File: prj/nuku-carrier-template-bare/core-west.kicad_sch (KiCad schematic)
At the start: 3 parts, among them J3 DF40HC(4.0)-90DS-0.4V

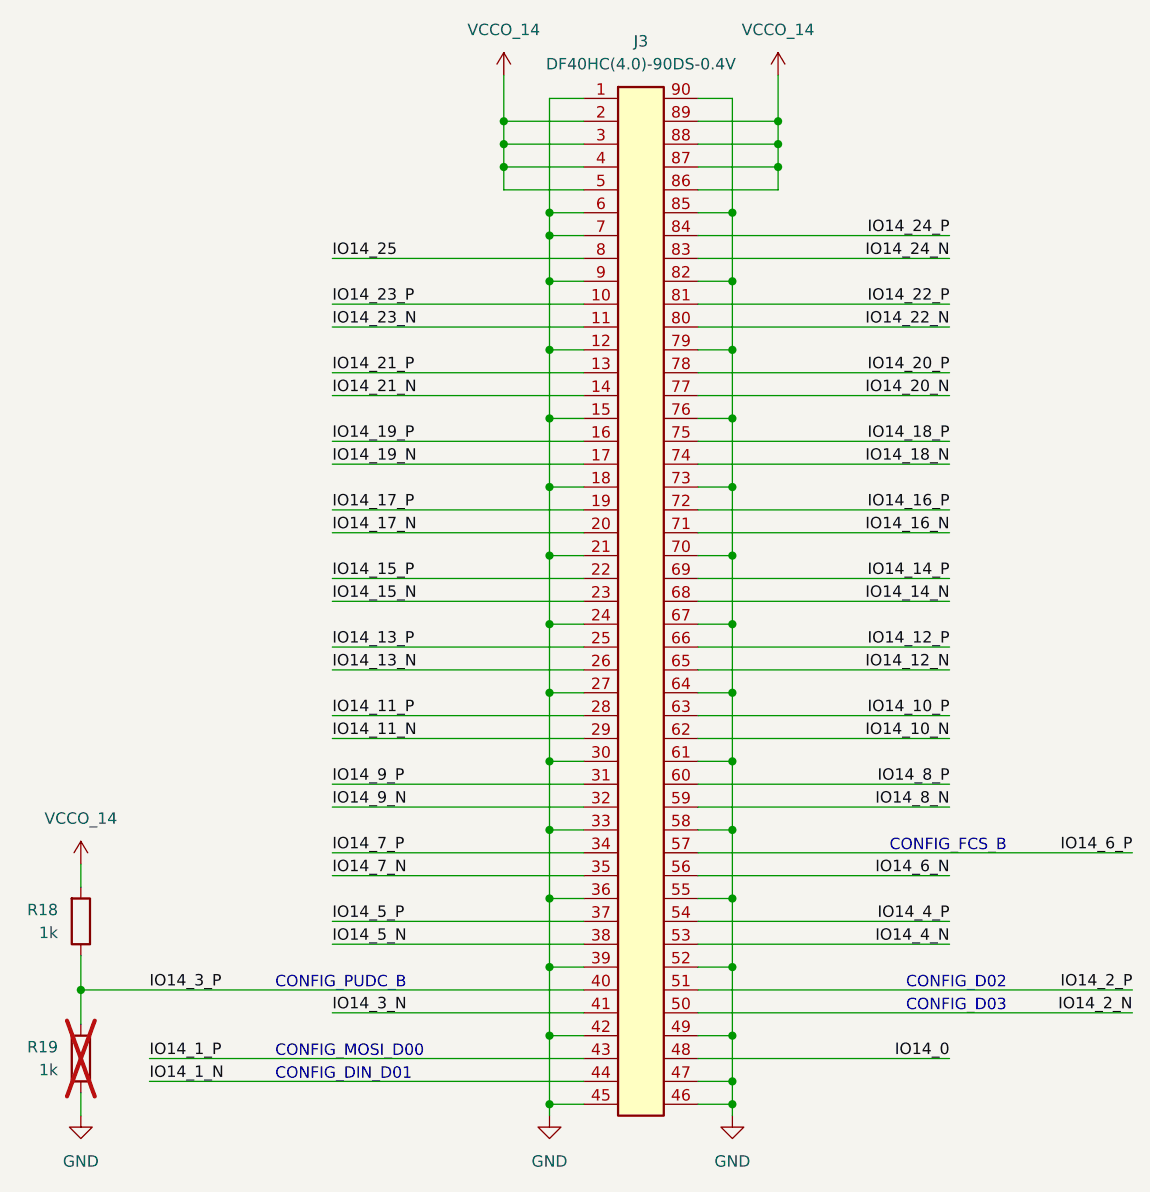
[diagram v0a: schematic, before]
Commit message: Update nuku.carrier.template to template.bare
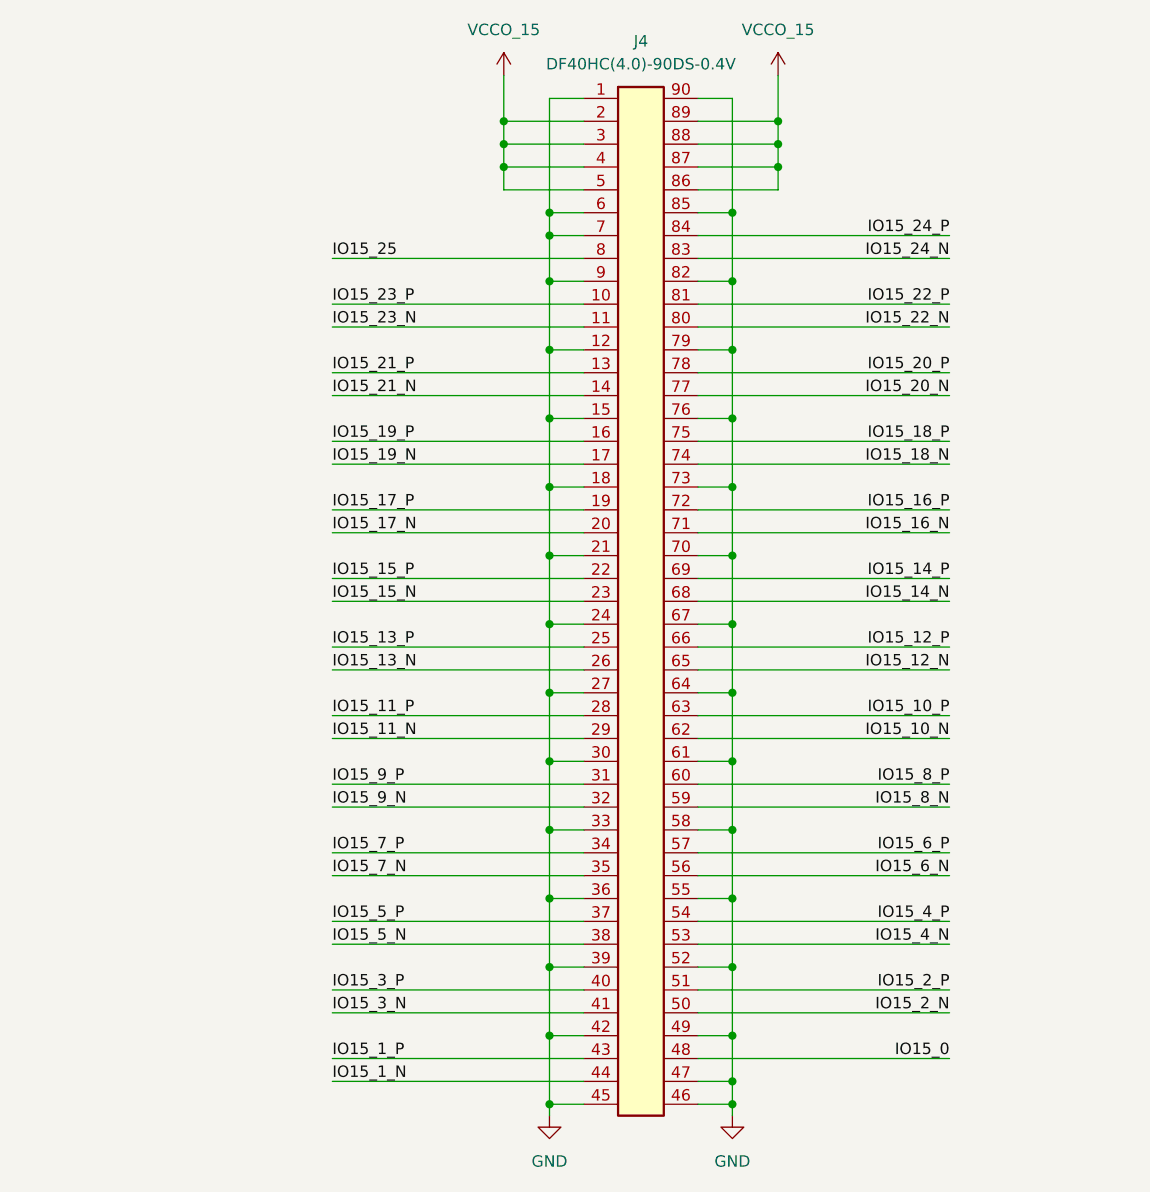
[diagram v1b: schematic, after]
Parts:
- removed J3: DF40HC(4.0)-90DS-0.4V, nuku:DF40HC(4.0)-90DS-0.4V, symbol nuku:DF40HC(4.0)-90DS-0.4V
- removed R18, R19: 1k, Resistor_SMD:R_0402_1005Metric, symbol Device:R
- added J4: DF40HC(4.0)-90DS-0.4V, nuku:DF40HC(4.0)-90DS-0.4V, symbol nuku:DF40HC(4.0)-90DS-0.4V
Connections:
- net GND: now also J4.1, J4.12, J4.15, J4.18, J4.21, J4.24, J4.27, J4.30, J4.33, J4.36, J4.39, J4.42, J4.45, J4.46, J4.47, J4.49, J4.52, J4.55, J4.58, J4.6, J4.61, J4.64, J4.67, J4.7, J4.70, J4.73, J4.76, J4.79, J4.82, J4.85, J4.9, J4.90
- new net IO15_0: J4.48
- new net IO15_10_N: J4.62
- new net IO15_10_P: J4.63
- new net IO15_11_N: J4.29
- new net IO15_11_P: J4.28
- new net IO15_12_N: J4.65
- new net IO15_12_P: J4.66
- new net IO15_13_N: J4.26
- new net IO15_13_P: J4.25
- new net IO15_14_N: J4.68
- new net IO15_14_P: J4.69
- new net IO15_15_N: J4.23
- new net IO15_15_P: J4.22
- new net IO15_16_N: J4.71
- new net IO15_16_P: J4.72
- new net IO15_17_N: J4.20
- new net IO15_17_P: J4.19
- new net IO15_18_N: J4.74
- new net IO15_18_P: J4.75
- new net IO15_19_N: J4.17
- new net IO15_19_P: J4.16
- new net IO15_1_N: J4.44
- new net IO15_1_P: J4.43
- new net IO15_20_N: J4.77
- new net IO15_20_P: J4.78
- new net IO15_21_N: J4.14
- new net IO15_21_P: J4.13
- new net IO15_22_N: J4.80
- new net IO15_22_P: J4.81
- new net IO15_23_N: J4.11
- new net IO15_23_P: J4.10
- new net IO15_24_N: J4.83
- new net IO15_24_P: J4.84
- new net IO15_25: J4.8
- new net IO15_2_N: J4.50
- new net IO15_2_P: J4.51
- new net IO15_3_N: J4.41
- new net IO15_3_P: J4.40
- new net IO15_4_N: J4.53
- new net IO15_4_P: J4.54
- new net IO15_5_N: J4.38
- new net IO15_5_P: J4.37
- new net IO15_6_N: J4.56
- new net IO15_6_P: J4.57
- new net IO15_7_N: J4.35
- new net IO15_7_P: J4.34
- new net IO15_8_N: J4.59
- new net IO15_8_P: J4.60
- new net IO15_9_N: J4.32
- new net IO15_9_P: J4.31
- new net VCCO_15: J4.2, J4.3, J4.4, J4.5, J4.86, J4.87, J4.88, J4.89
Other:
- note removed: "CONFIG_D02"
- note removed: "CONFIG_D03"
- note removed: "CONFIG_DIN_D01"
- note removed: "CONFIG_FCS_B"
- note removed: "CONFIG_MOSI_D00"
- note removed: "CONFIG_PUDC_B"
- company: (none) -> Samuel López Asunción
- title: (none) -> nuku.carrier.template.bare / core-west-15
